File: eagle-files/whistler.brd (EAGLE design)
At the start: 43.2 x 72.4 mm, 34 parts, among them U2 MLX90614_

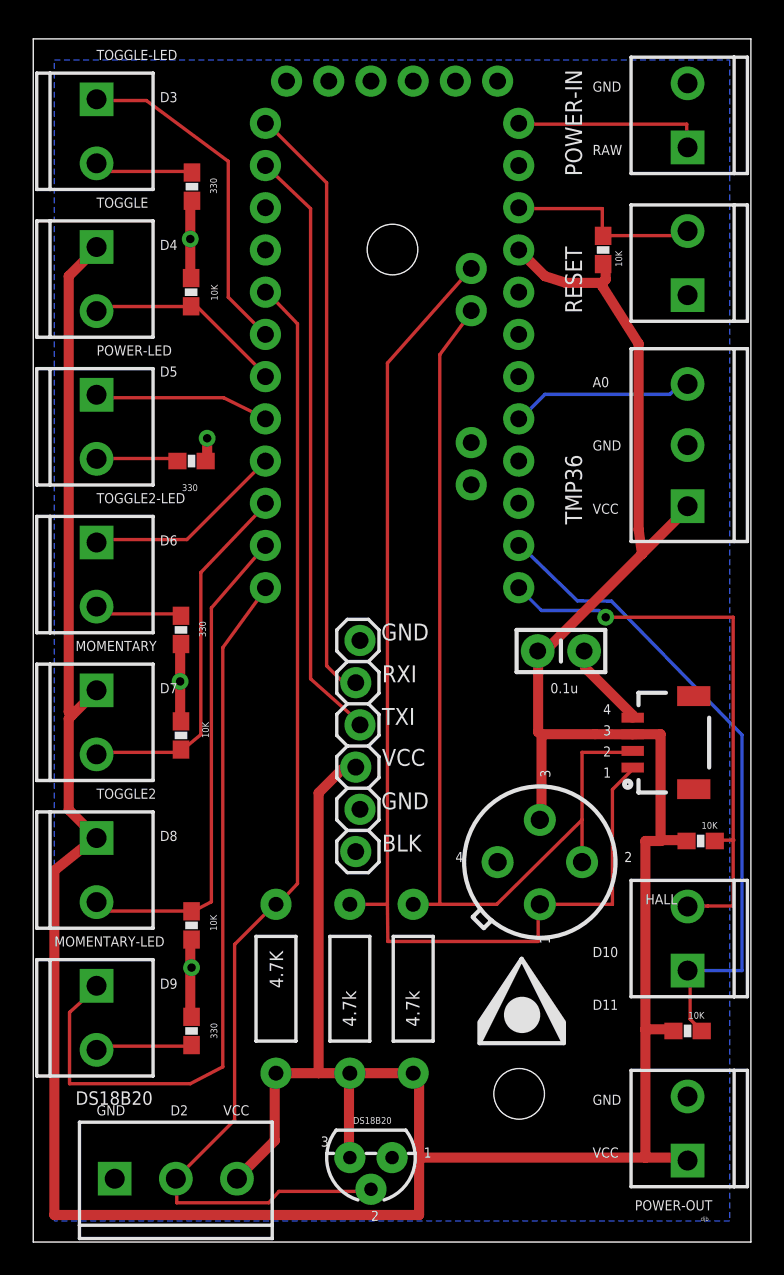
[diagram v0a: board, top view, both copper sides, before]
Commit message: changes to the silk layers in eagle.
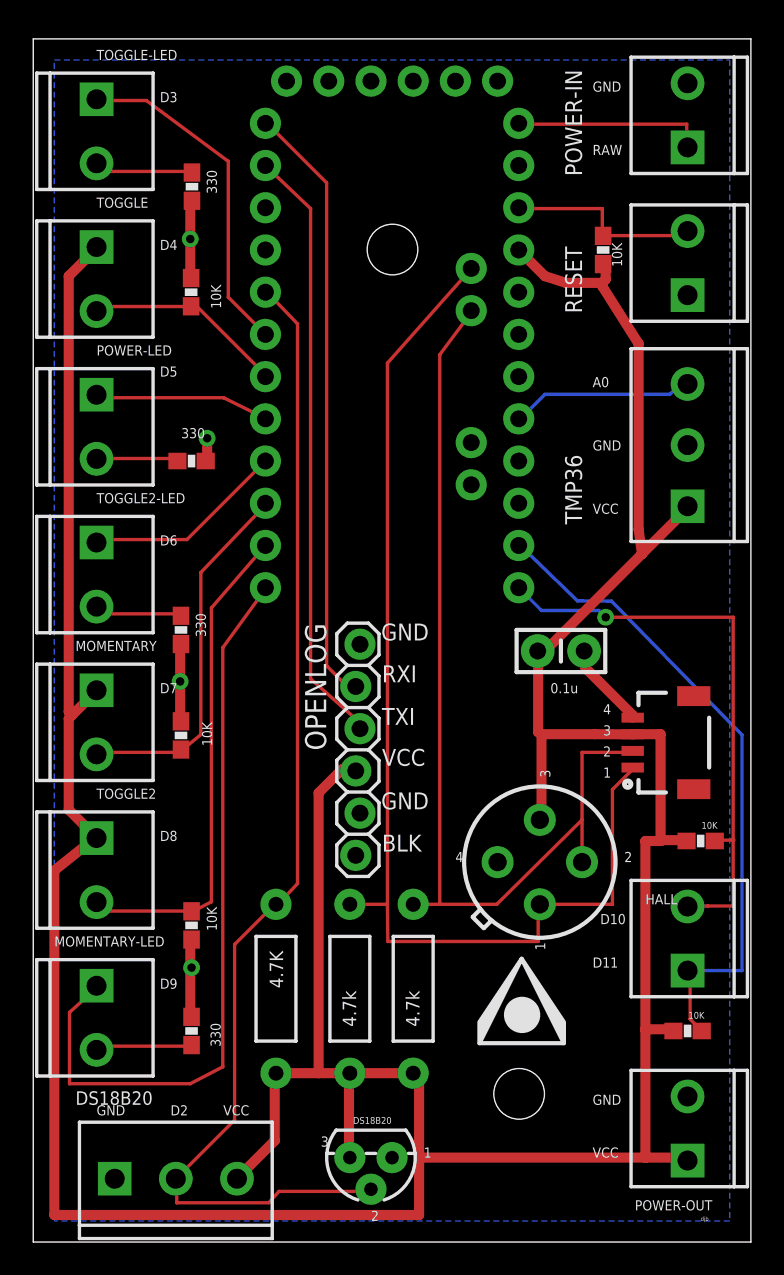
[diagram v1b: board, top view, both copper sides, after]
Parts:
- moved OPENLOG1 0.23 mm to (17.1, 41.0)
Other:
- board text added: "MOMENTARY LED"
- board text added: "WHISTLER"
- board text removed: "MOMEN TARY"
- board text removed: "MOMENT ARY LED"
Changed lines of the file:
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@@
 <text x="31.115" y="10.16" size="0.6096" layer="21">VCC</text>
 <text x="31.115" y="13.335" size="0.6096" layer="21">GND</text>
-<text x="31.115" y="22.225" size="0.6096" layer="21">D10</text>
-<text x="31.115" y="19.05" size="0.6096" layer="21">D11</text>
+<text x="31.5722" y="24.2062" size="0.6096" layer="21">D10</text>
+<text x="31.115" y="21.59" size="0.6096" layer="21">D11</text>
 <text x="5.08" y="73.66" size="0.6096" layer="21">D3</text>
 <text x="5.08" y="57.15" size="0.6096" layer="21">D5</text>
@@
 <text x="1.27" y="12.7" size="0.6096" layer="21">GND</text>
 <text x="34.29" y="25.4" size="0.6096" layer="21">HALL</text>
-<text x="2.54" y="59.69" size="1.27" layer="22" rot="MR90">TOGGLE</text>
-<text x="2.54" y="68.58" size="1.27" layer="22" rot="MR90">TOGGLE
+<text x="-1.27" y="63.5" size="1.27" layer="22" rot="MR180">TOGGLE</text>
+<text x="-1.27" y="72.39" size="1.27" layer="22" rot="MR180">TOGGLE
 LED</text>
-<text x="2.54" y="51.435" size="1.27" layer="22" rot="MR90">POWER
+<text x="0" y="54.5846" size="1.27" layer="22" rot="MR180">POWER
 LED</text>
-<text x="2.54" y="41.91" size="1.27" layer="22" rot="MR90">TOGGLE2
+<text x="-1.27" y="45.72" size="1.27" layer="22" rot="MR180">TOGGLE2
 LED</text>
-<text x="2.54" y="33.02" size="1.27" layer="22" rot="MR90">MOMEN
-TARY</text>
-<text x="2.54" y="14.605" size="1.27" layer="22" rot="MR90">MOMENT
-ARY LED</text>
-<text x="2.54" y="23.495" size="1.27" layer="22" rot="MR90">TOGGLE2</text>
-<text x="10.16" y="10.16" size="1.27" layer="22" rot="MR0">DS18B20</text>
-<text x="32.385" y="8.89" size="1.27" layer="22" rot="MR90">POWER
+<text x="-1.27" y="36.83" size="1.27" layer="22" rot="MR180">MOMENTARY</text>
+<text x="-1.27" y="19.05" size="1.27" layer="22" rot="MR180">MOMENTARY
+LED</text>
+<text x="-1.27" y="27.94" size="1.27" layer="22" rot="MR180">TOGGLE2</text>
+<text x="10.16" y="10.7442" size="1.27" layer="22" rot="MR0">DS18B20</text>
+<text x="29.21" y="12.7" size="1.27" layer="22" rot="MR180">POWER
 OUT</text>
-<text x="34.29" y="17.78" size="1.27" layer="22" rot="MR90">HALL</text>
-<text x="34.29" y="50.8" size="1.27" layer="22" rot="MR90">TMP36</text>
-<text x="34.29" y="60.96" size="1.27" layer="22" rot="MR90">RESET</text>
-<text x="32.385" y="69.85" size="1.27" layer="22" rot="MR90">POWER
+<text x="39.37" y="22.86" size="1.27" layer="22" rot="MR0">HALL</text>
+<text x="35.56" y="54.61" size="1.27" layer="22" rot="MR0">TMP36</text>
+<text x="39.37" y="63.5" size="1.27" layer="22" rot="MR0">RESET</text>
+<text x="34.3662" y="73.6346" size="1.27" layer="22" rot="MR180">POWER
 IN</text>
 <text x="20.955" y="10.16" size="0.6096" layer="21">1</text>
 <text x="17.78" y="6.35" size="0.6096" layer="21">2</text>
 <text x="15.24" y="11.43" size="0.6096" layer="21" rot="R180">3</text>
-<text x="27.94" y="23.495" size="0.6096" layer="21" rot="R270">1</text>
+<text x="27.6606" y="23.114" size="0.6096" layer="21" rot="R270">1</text>
 <text x="33.02" y="27.94" size="0.6096" layer="21">2</text>
 <text x="28.575" y="33.02" size="0.6096" layer="21" rot="R90">3</text>
@@
 <text x="31.75" y="35.56" size="0.6096" layer="21">3</text>
 <text x="31.75" y="36.83" size="0.6096" layer="21">4</text>
+<text x="36.83" y="33.02" size="3.81" layer="22" rot="MR0">WHISTLER</text>
 </plain>
 <attributes>
@@
 </element>
 <element name="DS18B20" library="SparkFun-Sensors" package="TO-92" value="" x="17.78" y="10.16" smashed="yes" rot="R180">
-<attribute name="NAME" x="19.0246" y="12.5984" size="0.4064" layer="25" ratio="10" rot="R180"/>
+<attribute name="NAME" x="19.0246" y="12.5984" size="0.4064" layer="21" ratio="10" rot="R180"/>
 <attribute name="VALUE" x="14.605" y="11.43" size="0.4064" layer="27" ratio="10" rot="R180"/>
 </element>
@@
 <attribute name="VALUE" x="35.56" y="69.85" size="0.4064" layer="27" rot="R90"/>
 </element>
-<element name="OPENLOG1" library="SparkFun" package="1X06_LOCK" value="OPENLOG" x="17.1196" y="41.275" smashed="yes" rot="R270">
-<attribute name="VALUE" x="13.8176" y="42.545" size="1.27" layer="27" font="vector" rot="R270"/>
+<element name="OPENLOG1" library="SparkFun" package="1X06_LOCK" value="OPENLOG" x="17.1196" y="41.0464" smashed="yes" rot="R270">
+<attribute name="VALUE" x="13.8176" y="42.3164" size="1.27" layer="21" font="vector" rot="R270"/>
 </element>
 <element name="C2" library="SparkFun-Capacitors" package="CAP-PTH-SMALL-KIT" value=".1uF" x="29.21" y="40.64">
@@
 <element name="R10" library="SparkFun-Resistors" package="0603-RES" value="10K" x="6.9596" y="62.23" smashed="yes" rot="R270">
 <attribute name="PROD_ID" value="RES-00824" x="6.9596" y="62.23" size="1.778" layer="27" rot="R270" display="off"/>
-<attribute name="VALUE" x="8.1534" y="62.6872" size="0.4064" layer="21" font="vector" rot="R270"/>
+<attribute name="VALUE" x="8.1534" y="62.6872" size="0.6096" layer="21" font="vector" rot="R270"/>
 </element>
 <element name="R5" library="SparkFun-Resistors" package="0603-RES" value="330" x="7.0104" y="68.58" smashed="yes" rot="R90">
 <attribute name="PROD_ID" value="RES-00818" x="7.0104" y="68.58" size="1.778" layer="27" rot="R90" display="off"/>
-<attribute name="VALUE" x="8.509" y="68.1482" size="0.4064" layer="21" font="vector" rot="R90"/>
+<attribute name="VALUE" x="8.509" y="68.1482" size="0.6096" layer="21" font="vector" rot="R90"/>
 </element>
 <element name="R6" library="SparkFun-Resistors" package="0603-RES" value="330" x="6.985" y="52.07" smashed="yes" rot="R180">
 <attribute name="PROD_ID" value="RES-00818" x="6.985" y="52.07" size="1.778" layer="27" rot="R180" display="off"/>
-<attribute name="VALUE" x="7.366" y="50.673" size="0.4064" layer="21" font="vector" rot="R180"/>
+<attribute name="VALUE" x="7.7978" y="54.0512" size="0.6096" layer="21" font="vector" rot="R180"/>
 </element>
 <element name="R7" library="SparkFun-Resistors" package="0603-RES" value="330" x="6.35" y="41.91" smashed="yes" rot="R90">
 <attribute name="PROD_ID" value="RES-00818" x="6.35" y="41.91" size="1.778" layer="27" rot="R90" display="off"/>
-<attribute name="VALUE" x="7.8486" y="41.4782" size="0.4064" layer="21" font="vector" rot="R90"/>
+<attribute name="VALUE" x="7.8486" y="41.4782" size="0.6096" layer="21" font="vector" rot="R90"/>
 </element>
 <element name="MOMENTARY" library="SparkFun-Connectors" package="SCREWTERMINAL-3.5MM-2_LOCK" value="" x="1.27" y="38.1" smashed="yes" rot="R270">
@@
 <element name="R11" library="SparkFun-Resistors" package="0603-RES" value="10K" x="6.35" y="35.56" smashed="yes" rot="R270">
 <attribute name="PROD_ID" value="RES-00824" x="6.35" y="35.56" size="1.778" layer="27" rot="R270" display="off"/>
-<attribute name="VALUE" x="7.62" y="36.3728" size="0.4064" layer="21" font="vector" rot="R270"/>
+<attribute name="VALUE" x="7.62" y="36.3728" size="0.6096" layer="21" font="vector" rot="R270"/>
 </element>
 <element name="R12" library="SparkFun-Resistors" package="0603-RES" value="10K" x="6.985" y="24.13" smashed="yes" rot="R90">
 <attribute name="PROD_ID" value="RES-00824" x="6.985" y="24.13" size="1.778" layer="27" rot="R90" display="off"/>
-<attribute name="VALUE" x="8.509" y="23.7998" size="0.4064" layer="21" font="vector" rot="R90"/>
+<attribute name="VALUE" x="8.509" y="23.7998" size="0.6096" layer="21" font="vector" rot="R90"/>
 </element>
 <element name="VCC/GND" library="SparkFun-Connectors" package="SCREWTERMINAL-3.5MM-2_LOCK" value="" x="36.83" y="10.16" smashed="yes" rot="R90">
@@
 <element name="R8" library="SparkFun-Resistors" package="0603-RES" value="330" x="6.985" y="17.78" smashed="yes" rot="R270">
 <attribute name="PROD_ID" value="RES-00818" x="6.985" y="17.78" size="1.778" layer="27" rot="R270" display="off"/>
-<attribute name="VALUE" x="8.128" y="18.2626" size="0.4064" layer="21" font="vector" rot="R270"/>
+<attribute name="VALUE" x="8.128" y="18.2626" size="0.6096" layer="21" font="vector" rot="R270"/>
 </element>
 <element name="DS18B20-CON" library="SparkFun-Connectors" package="SCREWTERMINAL-3.5MM-3_LOCK.007S" value="CON" x="2.54" y="8.89" smashed="yes"/>
@@
 <element name="R13" library="SparkFun-Resistors" package="0603-RES" value="10K" x="31.75" y="64.77" smashed="yes" rot="R90">
 <attribute name="PROD_ID" value="RES-00824" x="31.75" y="64.77" size="1.778" layer="27" rot="R90" display="off"/>
-<attribute name="VALUE" x="32.893" y="63.754" size="0.4064" layer="21" font="vector" rot="R90"/>
+<attribute name="VALUE" x="32.893" y="63.754" size="0.6096" layer="21" font="vector" rot="R90"/>
 </element>
 <element name="TMP36" library="SparkFun-Connectors" package="SCREWTERMINAL-3.5MM-3_LOCK.007S" value="TMP36" x="36.83" y="49.53" smashed="yes" rot="R90"/>
@@
 <wire x1="15.113" y1="68.8086" x2="15.113" y2="39.751" width="0.2032" layer="1"/>
 <wire x1="11.5824" y1="72.3392" x2="15.113" y2="68.8086" width="0.2032" layer="1"/>
-<wire x1="16.0528" y1="38.8112" x2="16.8656" y2="38.735" width="0.2032" layer="1"/>
+<wire x1="16.0528" y1="38.8112" x2="16.8656" y2="38.5064" width="0.2032" layer="1"/>
 <wire x1="11.5824" y1="72.3392" x2="11.43" y2="72.39" width="0.2032" layer="1"/>
 </signal>
@@
 <wire x1="14.6304" y1="32.1056" x2="16.0528" y2="33.528" width="0.6096" layer="1"/>
 <wire x1="14.6304" y1="15.24" x2="14.6304" y2="32.1056" width="0.6096" layer="1"/>
-<wire x1="16.0528" y1="33.528" x2="16.8656" y2="33.655" width="0.6096" layer="1"/>
+<wire x1="16.0528" y1="33.528" x2="16.8656" y2="33.4264" width="0.6096" layer="1"/>
 <wire x1="16.51" y1="15.24" x2="20.32" y2="15.24" width="0.6096" layer="1"/>
 <wire x1="11.9888" y1="11.176" x2="9.7536" y2="8.9408" width="0.6096" layer="1"/>
@@
 <wire x1="14.1478" y1="67.2592" x2="14.1478" y2="38.9636" width="0.2032" layer="1"/>
 <wire x1="11.43" y1="69.85" x2="14.1478" y2="67.2592" width="0.2032" layer="1"/>
-<wire x1="17.0688" y1="36.3728" x2="17.1196" y2="36.195" width="0.2032" layer="1"/>
+<wire x1="17.0688" y1="36.3728" x2="17.1196" y2="35.9664" width="0.2032" layer="1"/>
 </signal>
 </signals>
